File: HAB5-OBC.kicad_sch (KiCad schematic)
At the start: 1 part, among them U1 STM32F411CEU6

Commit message: MCU core functionality
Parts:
- added C101, C111: 1206B475K500NT, EasyEDA:C1206, symbol EasyEDA:1206B475K500NT
- added C101, C102: 0402CG150J500NT, EasyEDA:C0402, symbol EasyEDA:0402CG150J500NT
- added C103, C104, C105, C106, C108, C109: CL05B104KO5NNNC, EasyEDA:C0402, symbol EasyEDA:CL05B104KO5NNNC
- added C107: CL21B105KBFNNNE, EasyEDA:C0805, symbol EasyEDA:CL21B105KBFNNNE
- added R101: 0402WGF1002TCE, EasyEDA:R0402, symbol EasyEDA:0402WGF1002TCE
- added SW101: TS-1088-AR02016, EasyEDA:SW-SMD_L3.9-W3.0-P4.45, symbol EasyEDA:TS-1088-AR02016
- added X101: 5032 8M 12PF 20PPM 4P, EasyEDA:CRYSTAL-SMD_4P-L5.0-W3.2-BL_ECS, symbol EasyEDA:50328M12PF20PPM4P
- renumbered U1 to U101
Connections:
- net +3V3: now reaches U101.1 (VBAT)
- net +3V3: now also U101.24 (VDD), U101.36 (VDD), U101.48 (VDD), U101.9 (VDDA/VREF+), C104.1, C105.1, C106.1, C107.1, C108.1, C109.1, C111.1
- net at U101.22 (VCAP1): now also C101.1
- net GND: now reaches U101.23 (VSS)
- net GND: now also U101.35 (VSS), U101.47 (VSS), U101.49 (PAD), U101.8 (VSSA/VREF-), C101.2, C101.2, C102.2, C103.2, C104.2, C105.2, C106.2, C107.2, C108.2, C109.2, C111.2, R101.2, SW101.2, X101.2 (GND), X101.4 (GND)
- net at U101.44 (BOOT0): now also R101.1
- net at U101.5 (PH0-OSC_IN): now also C102.1, X101.1
- net at U101.6 (PH1-OSC_OUT): now also C101.1, X101.3
- net at U101.7 (NRST): now also C103.1, SW101.1

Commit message: Interface Connections
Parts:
- added J101, J102, J103, J104: Conn_01x01_Pin, symbol Connector:Conn_01x01_Pin
- added R101, R102: 0603WAF4701T5E, EasyEDA:R0603, symbol EasyEDA:0603WAF4701T5E
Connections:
- net I2C1.SCL: now also R102.1
- net I2C1.SDA: now also R101.1
- net Temperature/LMT84_OUT: now reaches U101.10 (PA0)
- net Temperature/NTC_MID: now reaches U101.11 (PA1)
- net at U101.12 (PA2): now also J101.1 (Pin_1)
- net at U101.13 (PA3): now also J102.1 (Pin_1)
- net Data Handling/SPI1_CS_MICROSD: now reaches U101.14 (PA4)
- net SPI1.SCK: now reaches U101.15 (PA5)
- net SPI1.MISO: now reaches U101.16 (PA6)
- net SPI1.MOSI: now reaches U101.17 (PA7)
- net LED5: now reaches U101.20 (PB2)
- net SPI2.SCK: now reaches U101.21 (PB10)
- net Data Handling/SPI2_CS_NOR: now reaches U101.25 (PB12)
- net LED4: now reaches U101.26 (PB13)
- net SPI2.MISO: now reaches U101.27 (PB14)
- net SPI2.MOSI: now reaches U101.28 (PB15)
- net LED3: now reaches U101.29 (PA8)
- net USART1.TX: now reaches U101.30 (PA9)
- net USART1.RX: now reaches U101.31 (PA10)
- net LED0: now reaches U101.32 (PA11)
- net LED1: now reaches U101.33 (PA12)
- net SWD.SWDIO: now reaches U101.34 (PA13)
- net SWD.SWCLK: now reaches U101.37 (PA14)
- net LED2: now reaches U101.38 (PA15)
- net at U101.40 (PB4): now also J104.1 (Pin_1)
- net at U101.41 (PB5): now also J103.1 (Pin_1)
- net LED6: now reaches U101.45 (PB8)
- net LED7: now reaches U101.46 (PB9)
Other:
- sheet Data Handling ports: added SPI1_CS_MICROSD, SPI1{SCK MISO MOSI}, SPI2_CS_NOR, SPI2{SCK MISO MOSI}; removed none
- sheet Debug and Expansion ports: added LED[0..7], SWD{SWDIO SWCLK}, USART1{TX RX}; removed none
- sheet Positional Sheet ports: added I2C1{SDA SCL}; removed none
- sheet Temperature ports: added LMT84_OUT, NTC_MID; removed none

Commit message: change value for real value
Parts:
- C101, C111: value 1206B475K500NT -> 4.7uF
- C101, C102: value 0402CG150J500NT -> 15pF
- C103, C104, C105, C106, C108, C109: value CL05B104KO5NNNC -> 100nF
- C107: value CL21B105KBFNNNE -> 1uF
- R101: value 0402WGF1002TCE -> 10k
- R101, R102: value 0603WAF4701T5E -> 4.7k
- SW101: value TS-1088-AR02016 -> (none)
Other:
- moved on the sheet: C104, C105, C106, C111

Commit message: added NC flags
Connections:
- net GND: now also C101.1; no longer C101.2
- net at U101.6 (PH1-OSC_OUT), X101.3: now also C101.2; no longer C101.1
- no-connect marks 0 -> 3
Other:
- moved on the sheet: C101, C102, C103, C106, C107, C108, C109, SW101, X101

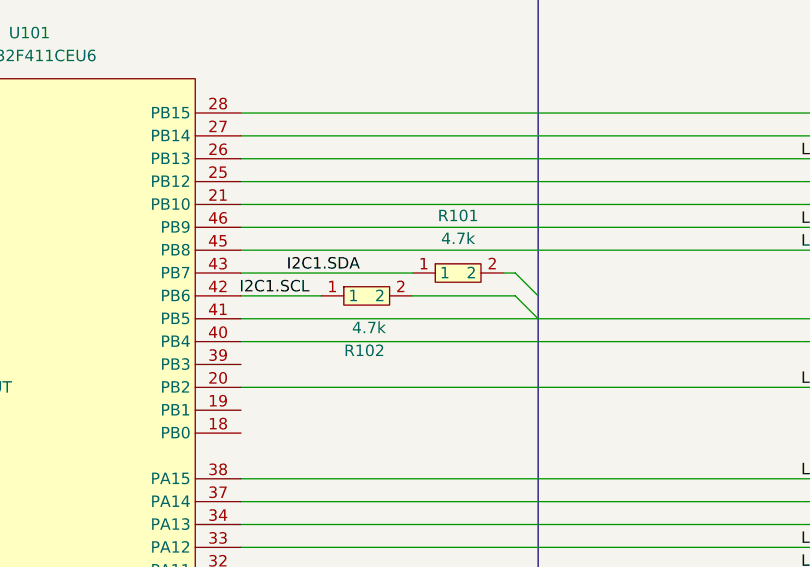
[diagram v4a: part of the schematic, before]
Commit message: Changed I2C pull up resistors
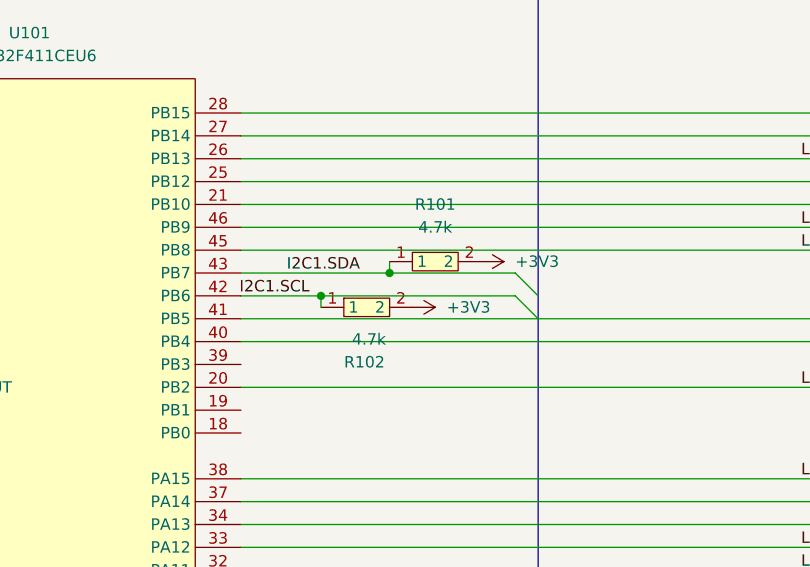
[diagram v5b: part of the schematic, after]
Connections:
- net +3V3: now also R101.2, R102.2
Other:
- moved on the sheet: R101, R102
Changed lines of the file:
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@@
 	)
 	(junction
+		(at 187.96 74.93)
+		(diameter 0)
+		(color 0 0 0 0)
+	)
+	(junction
 		(at 99.06 118.11)
 		(diameter 0)
@@
 	)
 	(junction
+		(at 180.34 77.47)
+		(diameter 0)
+		(color 0 0 0 0)
+	)
+	(junction
 		(at 125.73 57.15)
 		(diameter 0)
@@
 	(wire
 		(pts
+			(xy 187.96 74.93) (xy 201.93 74.93)
+		)
+		(stroke
+			(width 0)
+			(type default)
+		)
+	)
+	(wire
+		(pts
 			(xy 152.4 43.18) (xy 269.24 43.18)
 		)
@@
 	(wire
 		(pts
-			(xy 200.66 74.93) (xy 201.93 74.93)
+			(xy 171.45 77.47) (xy 180.34 77.47)
 		)
 		(stroke
@@
 		)
 	)
-	(wire
-		(pts
-			(xy 190.5 77.47) (xy 201.93 77.47)
-		)
-		(stroke
-			(width 0)
-			(type default)
-		)
-	)
 	(bus
 		(pts
@@
 	(wire
 		(pts
+			(xy 180.34 77.47) (xy 180.34 78.74)
+		)
+		(stroke
+			(width 0)
+			(type default)
+		)
+	)
+	(wire
+		(pts
 			(xy 256.54 105.41) (xy 256.54 102.87)
 		)
@@
 	(wire
 		(pts
+			(xy 187.96 73.66) (xy 187.96 74.93)
+		)
+		(stroke
+			(width 0)
+			(type default)
+		)
+	)
+	(wire
+		(pts
 			(xy 125.73 57.15) (xy 118.11 57.15)
 		)
@@
 	(wire
 		(pts
-			(xy 171.45 74.93) (xy 190.5 74.93)
-		)
-		(stroke
-			(width 0)
-			(type default)
-		)
-	)
-	(wire
-		(pts
-			(xy 171.45 77.47) (xy 180.34 77.47)
+			(xy 171.45 74.93) (xy 187.96 74.93)
 		)
 		(stroke
@@
 		)
 	)
+	(wire
+		(pts
+			(xy 180.34 77.47) (xy 201.93 77.47)
+		)
+		(stroke
+			(width 0)
+			(type default)
+		)
+	)
 	(label "USART1.RX"
 		(at 215.9 110.49 180)
@@
 	(symbol
 		(lib_id "EasyEDA:0603WAF4701T5E")
-		(at 185.42 77.47 0)
+		(at 185.42 78.74 0)
 		(unit 1)
 		(body_style 1)
@@
 		(dnp no)
 		(property "Reference" "R102"
-			(at 185.166 83.566 0)
+			(at 185.166 84.836 0)
 			(show_name no)
 			(do_not_autoplace no)
@@
 		)
 		(property "Value" "4.7k"
-			(at 185.674 81.026 0)
+			(at 185.674 82.296 0)
 			(show_name no)
 			(do_not_autoplace no)
@@
 		)
 		(property "Footprint" "EasyEDA:R0603"
-			(at 185.42 85.09 0)
+			(at 185.42 86.36 0)
 			(hide yes)
 			(show_name no)
@@
 		)
 		(property "Datasheet" "https://lcsc.com/product-detail/Chip-Resistor-Surface-Mount-UniOhm_4-7KR-4701-1_C23162.html"
-			(at 185.42 87.63 0)
+			(at 185.42 88.9 0)
 			(hide yes)
 			(show_name no)
@@
 		)
 		(property "Description" "4.7KΩ (4701) ±1%"
-			(at 185.42 77.47 0)
+			(at 185.42 78.74 0)
 			(hide yes)
 			(show_name no)
@@
 		)
 		(property "Manufacturer" "UNI-ROYAL(厚声)"
-			(at 185.42 90.17 0)
+			(at 185.42 91.44 0)
 			(hide yes)
 			(show_name no)
@@
 		)
 		(property "MPN" "0603WAF4701T5E"
-			(at 185.42 92.71 0)
+			(at 185.42 93.98 0)
 			(hide yes)
 			(show_name no)
@@
 		)
 		(property "LCSC Part" "C23162"
-			(at 185.42 95.25 0)
+			(at 185.42 96.52 0)
 			(hide yes)
 			(show_name no)
@@
 	)
 	(symbol
+		(lib_id "power:+3V3")
+		(at 190.5 78.74 270)
+		(unit 1)
+		(body_style 1)
+		(exclude_from_sim no)
+		(in_bom yes)
+		(on_board yes)
+		(in_pos_files yes)
+		(dnp no)
+		(fields_autoplaced yes)
+		(property "Reference" "#PWR0130"
+			(at 186.69 78.74 0)
+			(hide yes)
+			(show_name no)
+			(do_not_autoplace no)
+			(effects
+				(font
+					(size 1.27 1.27)
+				)
+			)
+		)
+		(property "Value" "+3V3"
+			(at 194.31 78.7399 90)
+			(show_name no)
+			(do_not_autoplace no)
+			(effects
+				(font
+					(size 1.27 1.27)
+				)
+				(justify left)
+			)
+		)
+		(property "Footprint" ""
+			(at 190.5 78.74 0)
+			(hide yes)
+			(show_name no)
+			(do_not_autoplace no)
+			(effects
+				(font
+					(size 1.27 1.27)
+				)
+			)
+		)
+		(property "Datasheet" ""
+			(at 190.5 78.74 0)
+			(hide yes)
+			(show_name no)
+			(do_not_autoplace no)
+			(effects
+				(font
+					(size 1.27 1.27)
+				)
+			)
+		)
+		(property "Description" "Power symbol creates a global label with name \"+3V3\""
+			(at 190.5 78.74 0)
+			(hide yes)
+			(show_name no)
+			(do_not_autoplace no)
+			(effects
+				(font
+					(size 1.27 1.27)
+				)
+			)
+		)
+		(pin "1"
+		)
+		(instances
+			(project "HAB5-OBC"
+				(path "/8bfdc6b4-3580-4cad-aef7-df6abccc03e5"
+					(reference "#PWR0130")
+					(unit 1)
+				)
+			)
+		)
+	)
+	(symbol
 		(lib_id "EasyEDA:1206B475K500NT")
 		(at 95.25 57.15 90)
@@
 	(symbol
 		(lib_id "EasyEDA:0603WAF4701T5E")
-		(at 195.58 74.93 0)
+		(at 193.04 73.66 0)
 		(unit 1)
 		(body_style 1)
@@
 		(fields_autoplaced yes)
 		(property "Reference" "R101"
-			(at 195.58 68.58 0)
+			(at 193.04 67.31 0)
 			(show_name no)
 			(do_not_autoplace no)
@@
 		)
 		(property "Value" "4.7k"
-			(at 195.58 71.12 0)
+			(at 193.04 69.85 0)
 			(show_name no)
 			(do_not_autoplace no)
@@
 		)
 		(property "Footprint" "EasyEDA:R0603"
-			(at 195.58 82.55 0)
+			(at 193.04 81.28 0)
 			(hide yes)
 			(show_name no)
@@
 		)
 		(property "Datasheet" "https://lcsc.com/product-detail/Chip-Resistor-Surface-Mount-UniOhm_4-7KR-4701-1_C23162.html"
-			(at 195.58 85.09 0)
+			(at 193.04 83.82 0)
 			(hide yes)
 			(show_name no)
@@
 		)
 		(property "Description" "4.7KΩ (4701) ±1%"
-			(at 195.58 74.93 0)
+			(at 193.04 73.66 0)
 			(hide yes)
 			(show_name no)
@@
 		)
 		(property "Manufacturer" "UNI-ROYAL(厚声)"
-			(at 195.58 87.63 0)
+			(at 193.04 86.36 0)
 			(hide yes)
 			(show_name no)
@@
 		)
 		(property "MPN" "0603WAF4701T5E"
-			(at 195.58 90.17 0)
+			(at 193.04 88.9 0)
 			(hide yes)
 			(show_name no)
@@
 		)
 		(property "LCSC Part" "C23162"
-			(at 195.58 92.71 0)
+			(at 193.04 91.44 0)
 			(hide yes)
 			(show_name no)
@@
 					(unit 1)
 				)
+			)
+		)
+	)
+	(symbol
+		(lib_id "power:+3V3")
+		(at 198.12 73.66 270)
+		(unit 1)
+		(body_style 1)
+		(exclude_from_sim no)
+		(in_bom yes)
+		(on_board yes)
+		(in_pos_files yes)
+		(dnp no)
+		(fields_autoplaced yes)
+		(property "Reference" "#PWR0128"
+			(at 194.31 73.66 0)
+			(hide yes)
+			(show_name no)
+			(do_not_autoplace no)
+			(effects
+				(font
+					(size 1.27 1.27)
+				)
+			)
+		)
+		(property "Value" "+3V3"
+			(at 201.93 73.6599 90)
+			(show_name no)
+			(do_not_autoplace no)
+			(effects
+				(font
+					(size 1.27 1.27)
+				)
+				(justify left)
+			)
+		)
+		(property "Footprint" ""
+			(at 198.12 73.66 0)
+			(hide yes)
+			(show_name no)
+			(do_not_autoplace no)
+			(effects
+				(font
+					(size 1.27 1.27)
+				)
+			)
+		)
+		(property "Datasheet" ""
+			(at 198.12 73.66 0)
+			(hide yes)
+			(show_name no)
+			(do_not_autoplace no)
+			(effects
+				(font
+					(size 1.27 1.27)
+				)
+			)
+		)
+		(property "Description" "Power symbol creates a global label with name \"+3V3\""
+			(at 198.12 73.66 0)
+			(hide yes)
+			(show_name no)
+			(do_not_autoplace no)
+			(effects
+				(font
+					(size 1.27 1.27)
+				)
+			)
+		)
+		(pin "1"
+		)
+		(instances
+			(project "HAB5-OBC"
+				(path "/8bfdc6b4-3580-4cad-aef7-df6abccc03e5"
+					(reference "#PWR0128")
+					(unit 1)
+				)
